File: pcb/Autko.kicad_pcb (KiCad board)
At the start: 2 copper layers, 140 x 155 mm, 124 parts, among them J1 PDI, M1 LEFT, M2 RIGHT, Q1 Si4368DY, Q2 BC817, SW1 POWER, SW2 START, SW3 STOP, U1 LTC3872, U10 CNY70, U11 TB6612FNG, U12 74HC14, U13 RN4678, U2 TLV1117-33, U3 ATxmega16A4U-A, U4 CNY70, U5 CNY70, U6 CNY70, U7 CNY70, U8 CNY70, U9 CNY70, Y1 8MHz

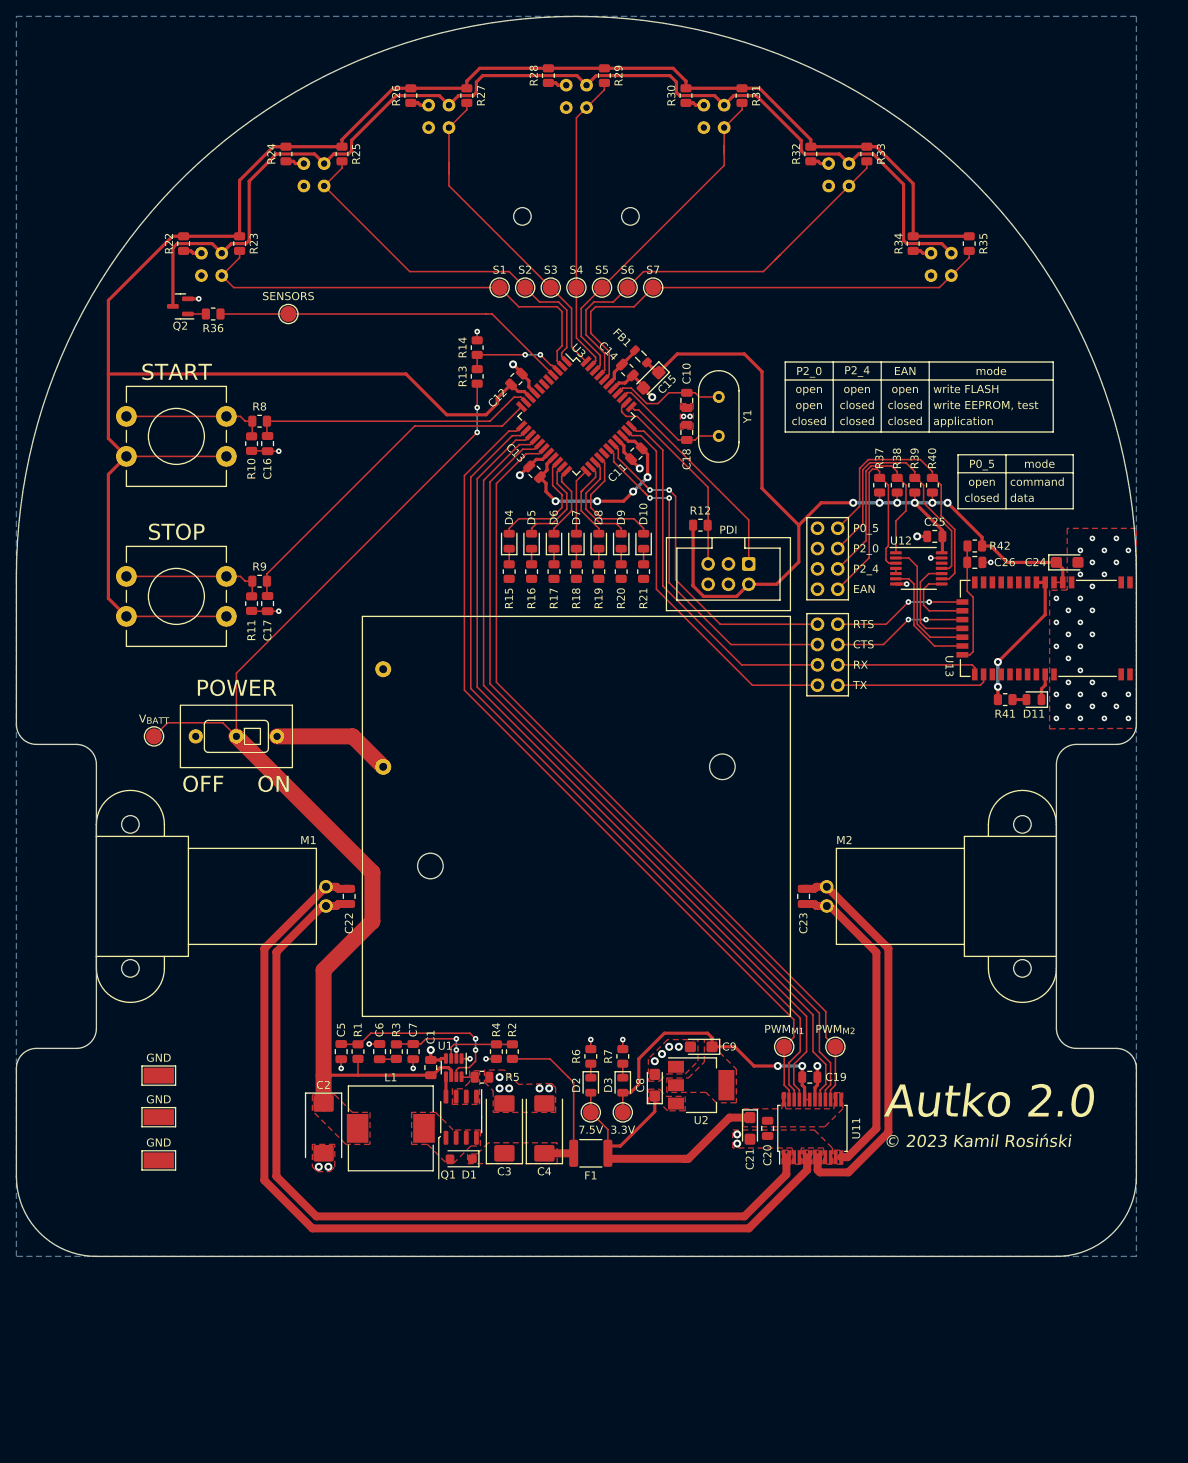
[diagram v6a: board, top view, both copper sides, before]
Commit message: [pcb] Alternative power routing
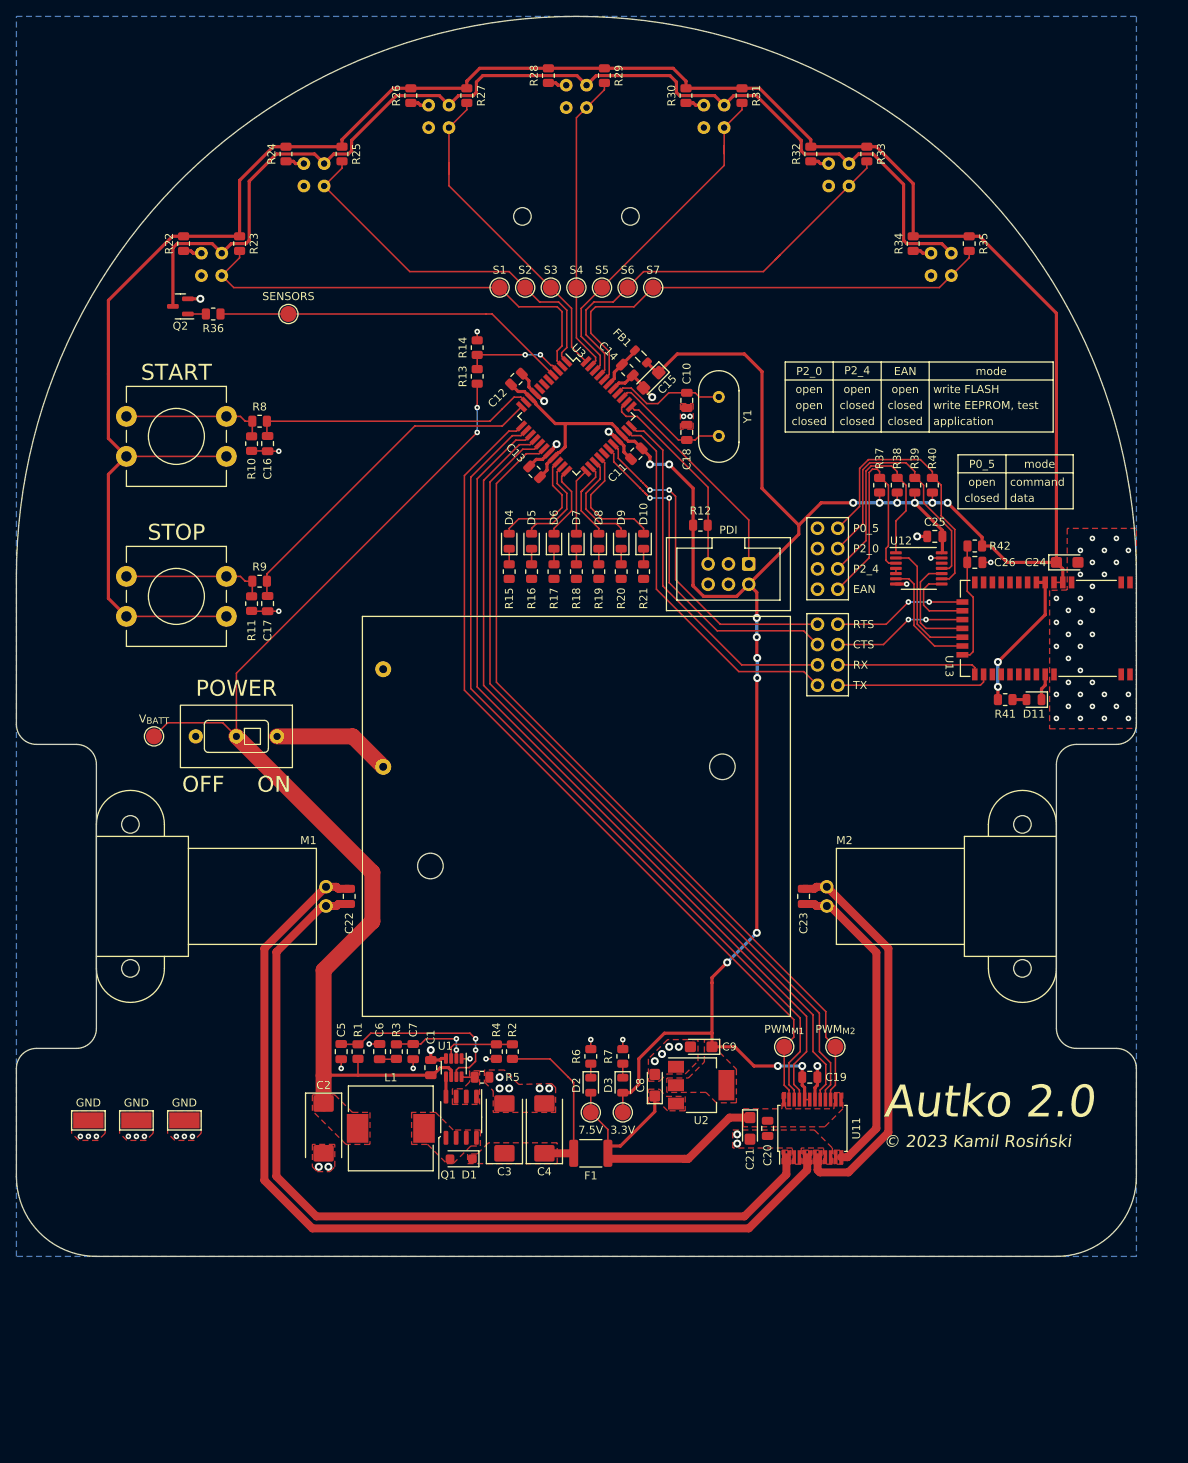
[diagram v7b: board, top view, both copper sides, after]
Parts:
- moved TP3 10.4 mm to (38.5, 168.5)
- moved TP4 5.94 mm to (50.5, 168.5)
- moved TP5 2.83 mm to (44.5, 168.5)
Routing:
- net +3.3V: track 446.6 -> 507.1 mm, vias 12 -> 16
- net GND: track 51.3 -> 51.2 mm, vias 71 -> 80

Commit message: [pcb] 4 layer PCB
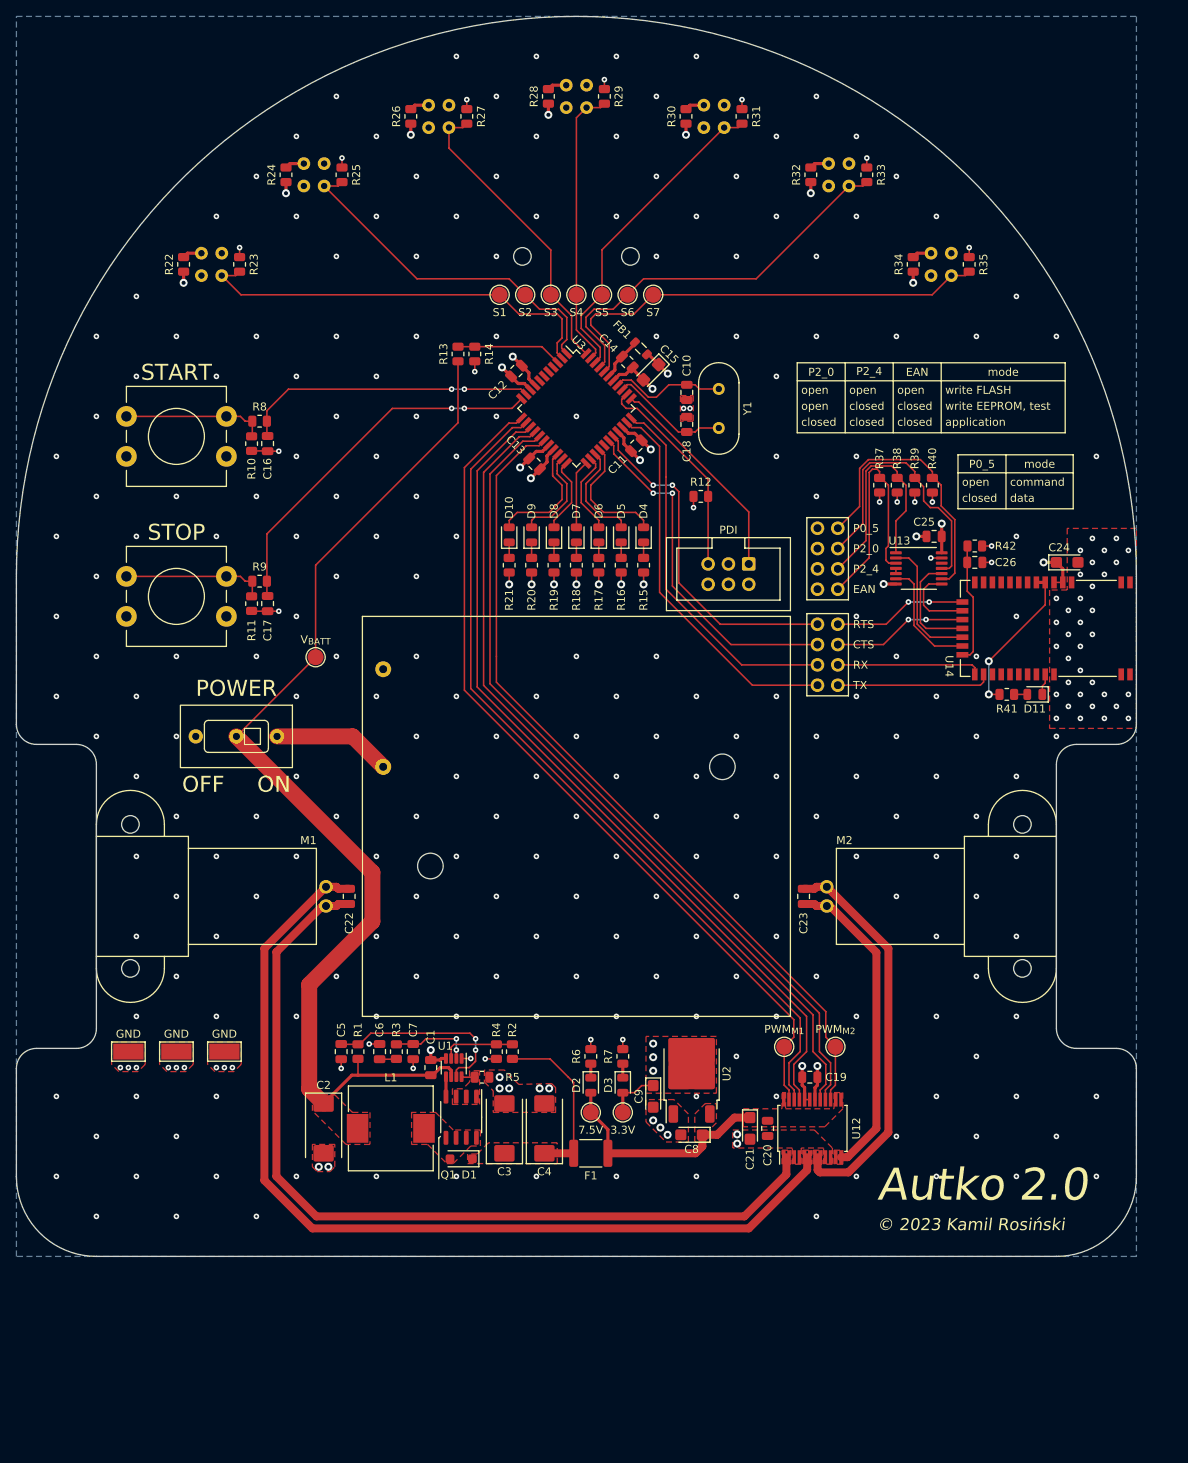
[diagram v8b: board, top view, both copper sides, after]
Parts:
- removed Q2: BC817, Package_TO_SOT_SMD:SOT-23
- removed R36: 10kR, Resistor_SMD:R_0805_2012Metric
- removed TP14: TestPoint, TestPoint:TestPoint_Pad_D2.0mm
- U2: footprint Package_TO_SOT_SMD:SOT-223-3_TabPin2 -> Package_TO_SOT_SMD:TO-252-2
- moved TP1 22.5 mm to (66.9, 110.6)
- moved R15 16.8 mm to (107.9, 99.1)
- moved R21 16.8 mm to (91.1, 99.1)
- moved D10 16.8 mm to (91.1, 95.3)
- moved D4 16.8 mm to (107.9, 95.3)
- moved D5 11.2 mm to (105.1, 95.3)
- moved D9 11.2 mm to (93.9, 95.3)
- moved R16 11.2 mm to (105.1, 99.1)
- moved R20 11.2 mm to (93.9, 99.1)
- moved TP3 9.95 mm to (43.5, 159.9)
- moved TP4 9.95 mm to (55.5, 159.9)
- moved TP5 9.95 mm to (49.5, 159.9)
- moved C9 8.63 mm to (109.1, 165.5), turned to -90 degrees
- moved C8 7.72 mm to (113.9, 170.3), turned to 180 degrees
- moved R17 5.66 mm to (102.3, 99.1)
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- renumbered U9 to U10, U10 to U11, U11 to U12, U12 to U13, U13 to U14, U4 to U5, U5 to U6, U6 to U7, U7 to U8, U8 to U9
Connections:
- U10 pad 2: Net-(Q2-C) -> GND
- U11 pad 2: Net-(Q2-C) -> GND
- U3 pad 20: /Microcontroller/LED1 -> /Microcontroller/LED7
- U3 pad 21: /Microcontroller/LED2 -> /Microcontroller/LED6
- U3 pad 22: /Microcontroller/LED3 -> /Microcontroller/LED5
- U3 pad 24: /Microcontroller/LED5 -> /Microcontroller/LED3
- U3 pad 25: /Microcontroller/LED6 -> /Microcontroller/LED2
- U3 pad 26: /Microcontroller/LED7 -> /Microcontroller/LED1
- U3 pad 4: /Line sensors/IR_LEDS_ON -> unconnected-(U3-AREFB/PB0-Pad4)
- U5 pad 2: Net-(Q2-C) -> GND
- U6 pad 2: Net-(Q2-C) -> GND
- U7 pad 2: Net-(Q2-C) -> GND
- U8 pad 2: Net-(Q2-C) -> GND
- U9 pad 2: Net-(Q2-C) -> GND
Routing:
- net +3.3V: track 507.1 -> 63.9 mm, vias 16 -> 30
- net Net-(Q2-C): track 140.2 -> 0.00 mm
- net /Line sensors/IR_LEDS_ON: track 44.8 -> 0.00 mm
- net GND: track 51.2 -> 60.9 mm, vias 80 -> 308
- net +7.5V: track 37.9 -> 28.9 mm
- net +BATT: track 143.1 -> 136.1 mm, vias 2 -> 0
- net /Line sensors/SENSOR3: track 41.7 -> 37.8 mm
- net /Line sensors/SENSOR6: track 53.5 -> 49.6 mm
- net /Line sensors/SENSOR5: track 44.0 -> 40.5 mm
- net /Microcontroller/BTN_STOP: track 43.3 -> 46.6 mm, vias 0 -> 2
- net /Line sensors/SENSOR7: track 60.7 -> 57.6 mm
- net /Line sensors/SENSOR2: track 47.7 -> 44.6 mm
- net /Line sensors/SENSOR1: track 55.7 -> 52.6 mm
- net /Line sensors/SENSOR4: track 38.3 -> 35.8 mm
- net Net-(Q2-B): track 2.25 -> 0.00 mm
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- added copper zone on B.Cu, net +3.3V
- added copper zone on In1.Cu, net GND
- added copper zone on In2.Cu, net GND
- removed copper zone on B.Cu, net GND
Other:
- copper layers 2 -> 4
